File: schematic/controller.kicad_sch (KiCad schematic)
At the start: 38 parts, among them J5 DB9_Male, J6 DB9_Male, Q4 2N3904, Q5 2N3904, U18 74LS541, U19 74LS541, U24 74LS00

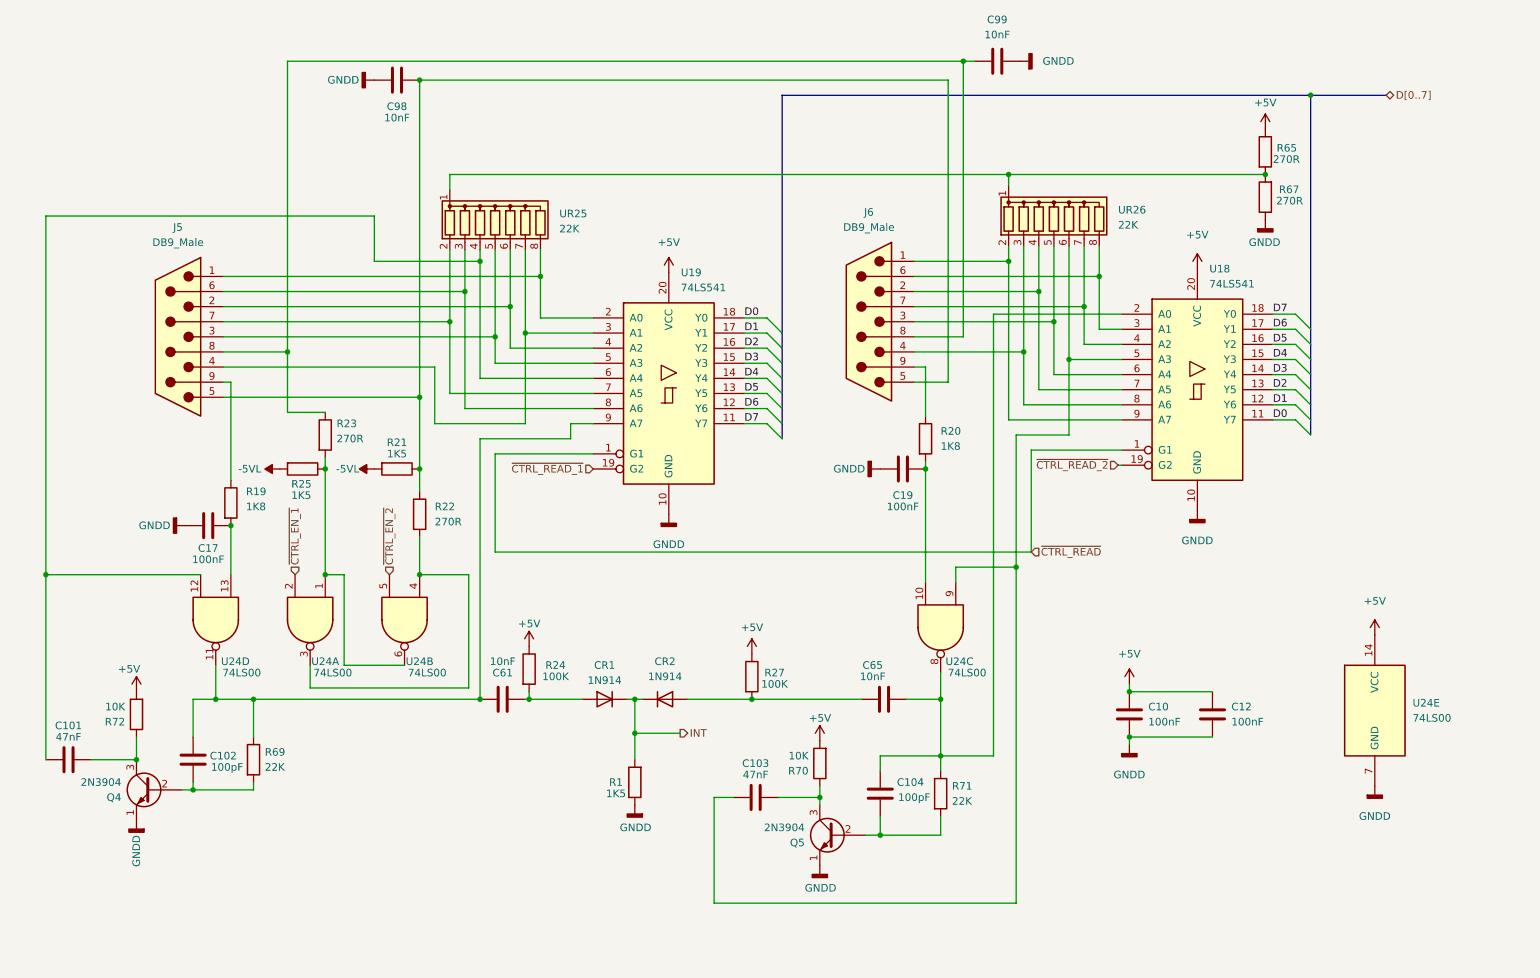
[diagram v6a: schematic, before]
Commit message: added pads for switch and RF shield, RF shield still needs adjustment
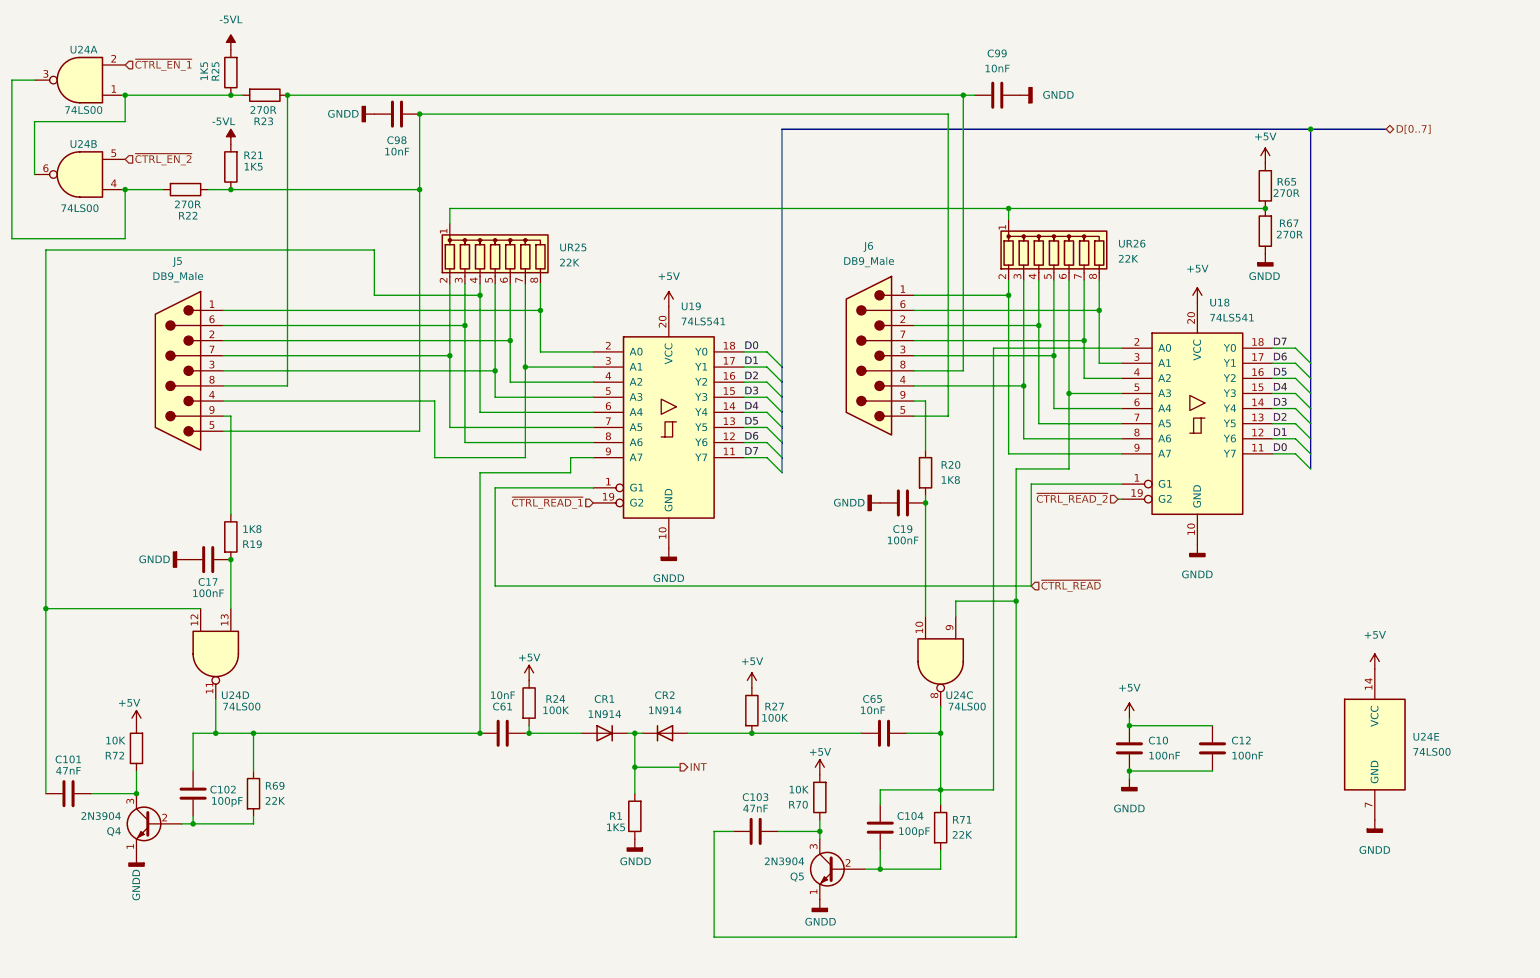
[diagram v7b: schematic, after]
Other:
- moved on the sheet: C10, C101, C102, C103, C104, C12, C17, C19, C61, C65, C98, C99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

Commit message: cleanup controller schematic
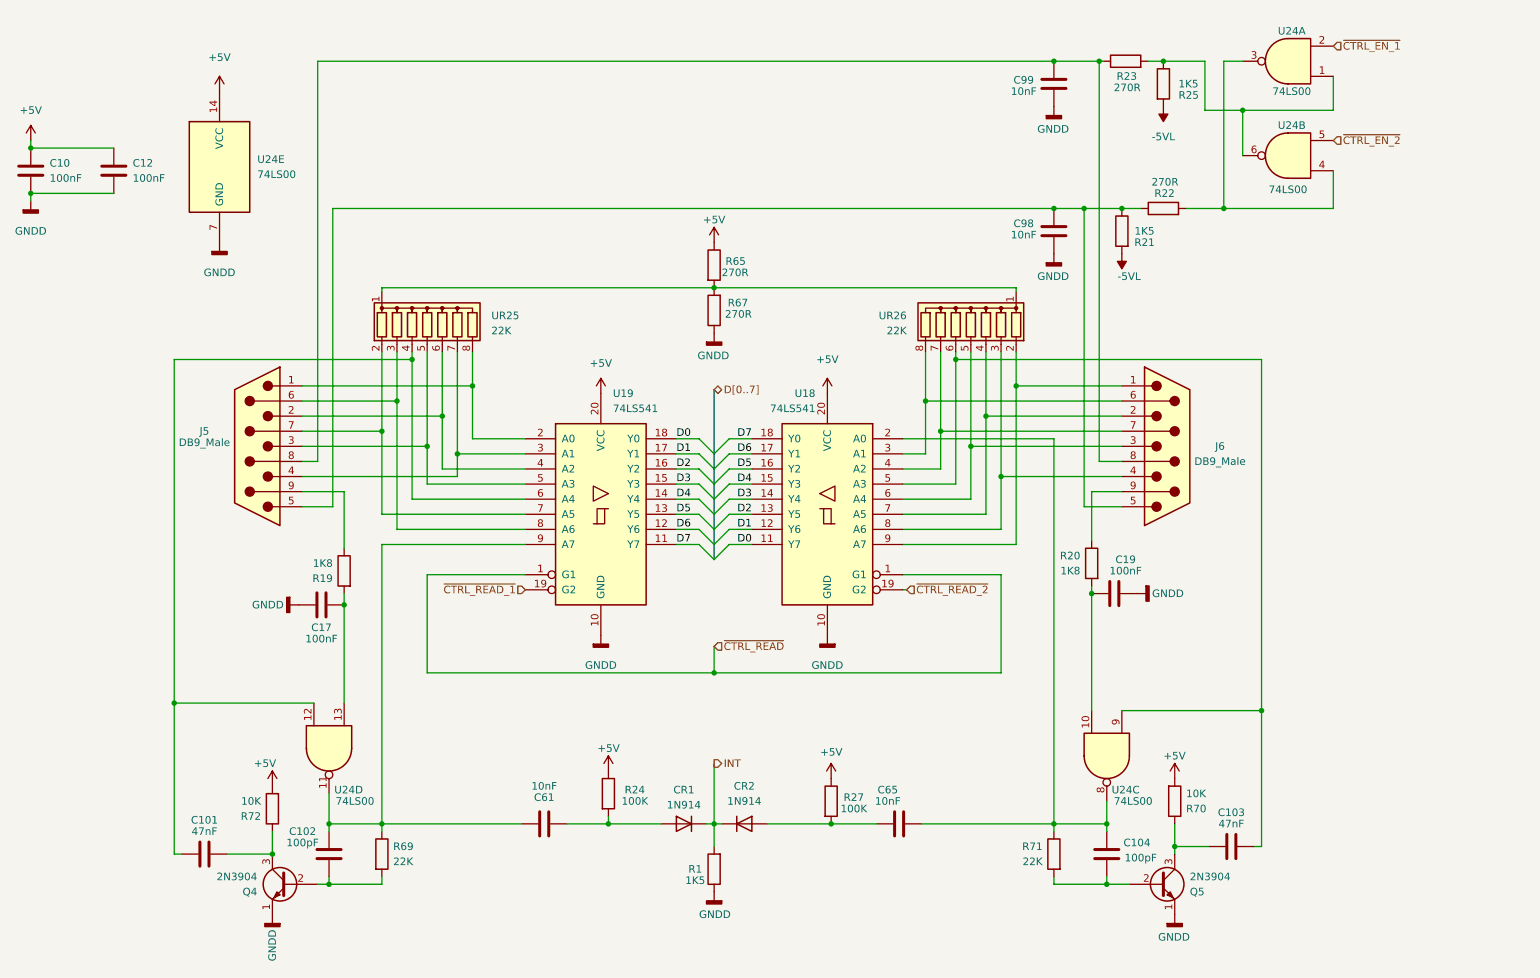
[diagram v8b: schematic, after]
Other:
- moved on the sheet: C10, C101, C102, C103, C104, C12, C17, C19, C61, C65, C98, C99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
